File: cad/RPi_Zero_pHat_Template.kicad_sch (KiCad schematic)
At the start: 2 parts, among them J1 RPi_GPIO, J2 RPi_GPIO

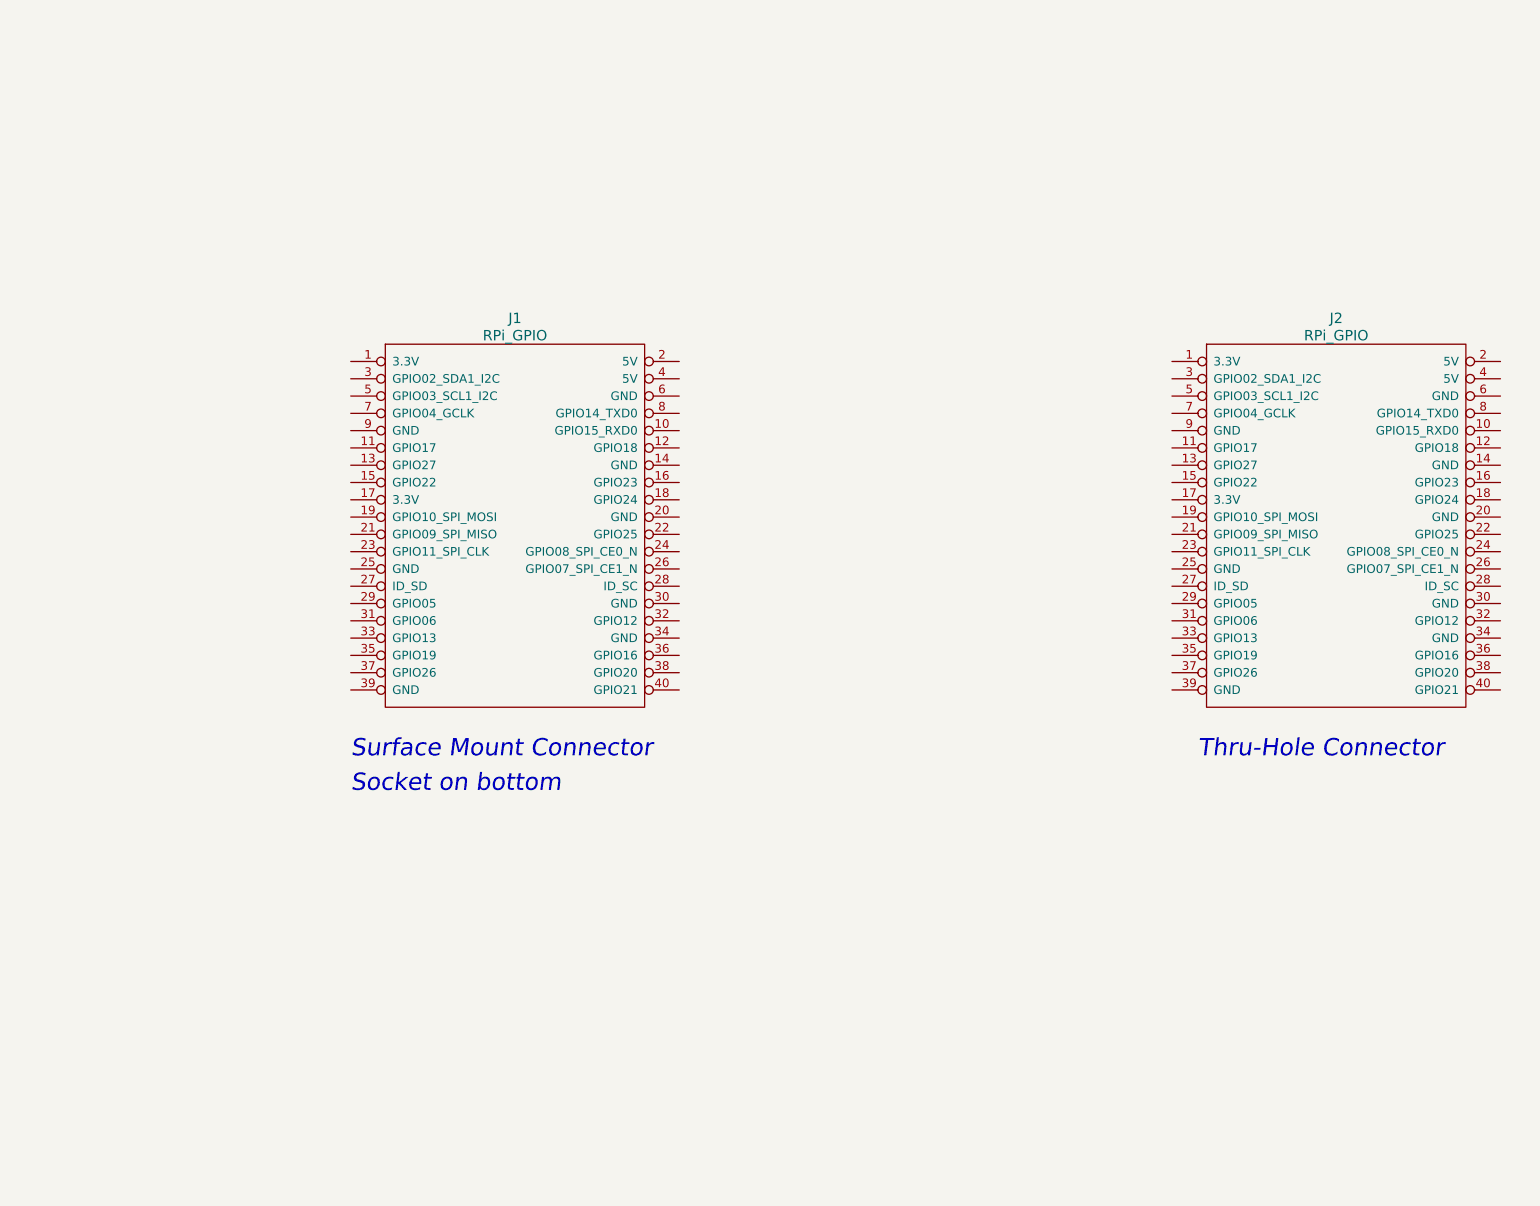
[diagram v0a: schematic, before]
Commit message: some headers added
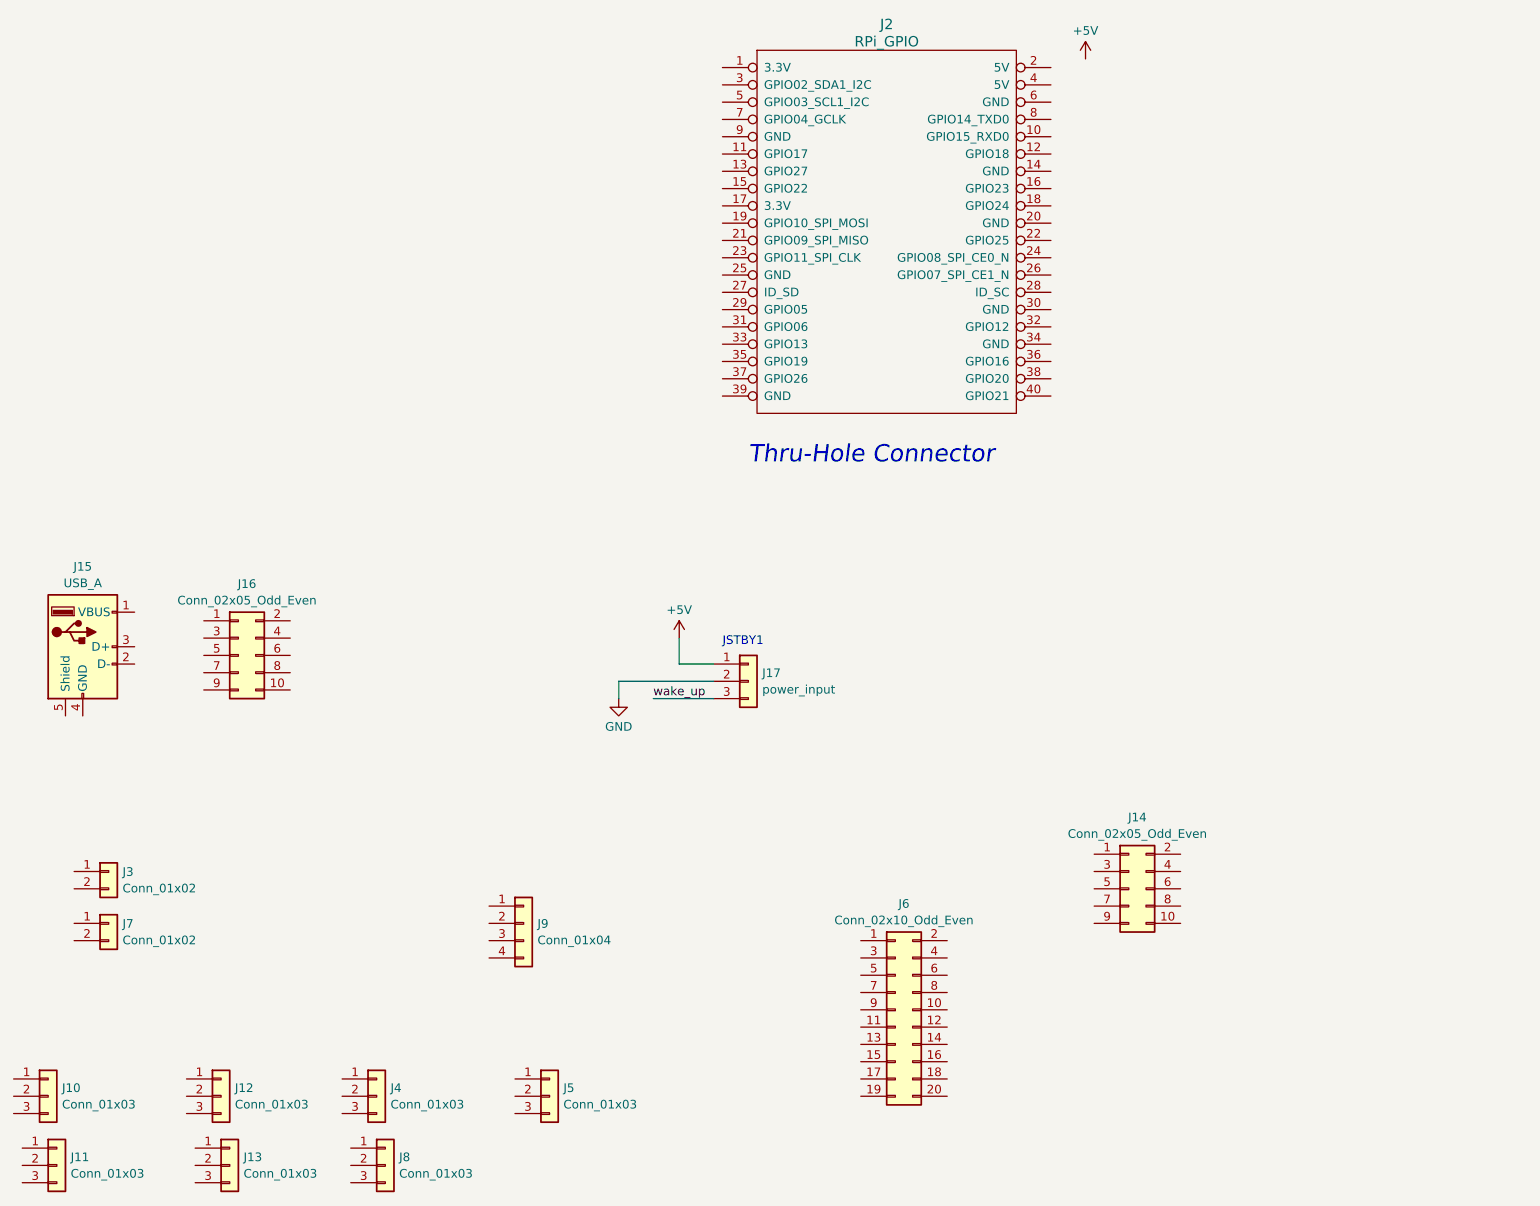
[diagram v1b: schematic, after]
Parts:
- removed J1: RPi_GPIO, RPi_Hat:Samtec_HLE-120-02-XXX-DV-BE-XX-XX, symbol RPi_Zero_pHat_Template-rescue:RPi_GPIO-Connector-ML
- added J10, J11, J12, J13, J4, J5, J8: Conn_01x03, Connector_PinHeader_2.54mm:PinHeader_1x03_P2.54mm_Vertical, symbol Connector_Generic:Conn_01x03
- added J14: Conn_02x05_Odd_Even, Connector_IDC:IDC-Header_2x05_P2.54mm_Vertical, symbol Connector_Generic:Conn_02x05_Odd_Even
- added J15: USB_A, Connector_USB:USB_A_CONNFLY_DS1095-WNR0, symbol Connector:USB_A
- added J16: Conn_02x05_Odd_Even, Connector_PinHeader_2.54mm:PinHeader_2x05_P2.54mm_Vertical, symbol Connector_Generic:Conn_02x05_Odd_Even
- added J17: power_input, Connector_PinHeader_2.54mm:PinHeader_1x03_P2.54mm_Vertical, symbol Connector_Generic:Conn_01x03
- added J3, J7: Conn_01x02, Connector_PinHeader_2.54mm:PinHeader_1x02_P2.54mm_Vertical, symbol Connector_Generic:Conn_01x02
- added J6: Conn_02x10_Odd_Even, Connector_PinHeader_2.54mm:PinHeader_2x10_P2.54mm_Vertical, symbol Connector_Generic:Conn_02x10_Odd_Even
- added J9: Conn_01x04, Connector_PinHeader_2.54mm:PinHeader_1x04_P2.54mm_Vertical, symbol Connector_Generic:Conn_01x04
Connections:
- new net +5V: J17.1 (Pin_1)
- new net GND: J17.2 (Pin_2)
- new net wake_up: J17.3 (Pin_3)
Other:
- note added: "JSTBY1"
- note removed: "Socket on bottom"
- note removed: "Surface Mount Connector"
- moved on the sheet: J2

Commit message: init
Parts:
- added D101, D102, D103, D104, D105, D106, D107, D108, D109, D110, D111, D112, D113, D114: led_g, LED_SMD:LED_0603_1608Metric, symbol Device:LED
- added R101, R102, R103, R104, R105, R106, R107, R108, R117, R118, R119, R120, R121, R122: 4.7k, Resistor_SMD:R_0603_1608Metric, symbol Device:R_Small
- added R109, R110, R111, R112, R113, R114, R115, R116, R123, R124, R125, R126, R127, R128: 10k, Resistor_SMD:R_0603_1608Metric, symbol Device:R_Small
- added U101, U102, U103, U104, U105, U106, U107, U108, U109, U110, U111, U112, U113, U114: ASSR-1218, Package_SO:SO-4_4.4x4.3mm_P2.54mm, symbol Relay_SolidState:ASSR-1218
- renumbered J10 to J101, J12 to J102, J5 to J103, J11 to J104, J4 to J105, J13 to J106, J8 to J107, J15 to J108, J3 to J109, J7 to J110, J16 to J111, J9 to J112, J17 to J113, J2 to J114, J6 to J115, J14 to J116
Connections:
- net +5V: now also J114.2 (5V), J114.4 (5V)
- net GND: now also R109.1, R110.1, R111.1, R112.1, R113.1, R114.1, R115.1, R116.1, R123.1, R124.1, R125.1, R126.1, R127.1, R128.1, U101.2, U102.2, U103.2, U104.2, U105.2, U106.2, U107.2, U108.2, U109.2, U110.2, U111.2, U112.2, U113.2, U114.2
- net at J106.1 (Pin_1): now also U111.4
- net at J106.2 (Pin_2): now also U111.3, U112.4
- net at J106.3 (Pin_3): now also U112.3
- net at J102.1 (Pin_1): now also U103.4
- net at J102.2 (Pin_2): now also U103.3, U104.4
- net at J102.3 (Pin_3): now also U104.3
- net at J101.1 (Pin_1): now also U101.4
- net at J101.2 (Pin_2): now also U101.3, U102.4
- net at J101.3 (Pin_3): now also U102.3
- net at J104.1 (Pin_1): now also U107.4
- net at J104.2 (Pin_2): now also U107.3, U108.4
- net at J104.3 (Pin_3): now also U108.3
- net at J103.1 (Pin_1): now also U105.4
- net at J103.2 (Pin_2): now also U105.3, U106.4
- net at J103.3 (Pin_3): now also U106.3
- net at J105.1 (Pin_1): now also U109.4
- net at J105.2 (Pin_2): now also U109.3, U110.4
- net at J105.3 (Pin_3): now also U110.3
- net at J107.1 (Pin_1): now also U113.4
- net at J107.2 (Pin_2): now also U113.3, U114.4
- net at J107.3 (Pin_3): now also U114.3
- new net: R102.1, U102.1
- new net: D112.1 (K), R126.2
- new net: D112.2 (A), R120.2
- new net: D113.1 (K), R127.2
- new net: R119.1, U111.1
- new net: D102.2 (A), R102.2
- new net: D105.1 (K), R113.2
- new net: R117.1, U109.1
- new net: R103.1, U103.1
- new net: D109.1 (K), R123.2
- new net: R104.1, U104.1
- new net: D104.2 (A), R104.2
- new net: R121.1, U113.1
- new net: R107.1, U107.1
- new net: D108.1 (K), R116.2
- new net: R101.1, U101.1
- new net: R105.1, U105.1
- new net: D101.1 (K), R109.2
- new net: D103.1 (K), R111.2
- new net: D107.1 (K), R115.2
- new net: R120.1, U112.1
- new net: R106.1, U106.1
- new net: D106.1 (K), R114.2
- new net: D106.2 (A), R106.2
- new net: R118.1, U110.1
- new net: R122.1, U114.1
- new net: D111.1 (K), R125.2
- new net: D102.1 (K), R110.2
- new net: D110.1 (K), R124.2
- new net: D110.2 (A), R118.2
- new net: R108.1, U108.1
- new net: D108.2 (A), R108.2
- new net: D114.1 (K), R128.2
- new net: D104.1 (K), R112.2
- new net: D114.2 (A), R122.2
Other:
- moved on the sheet: J101, J102, J103, J104, J105, J106, J107, J108, J109, J110, J111, J112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

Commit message: check in before tpm
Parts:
- added C101: .1uF, Capacitor_SMD:C_0603_1608Metric, symbol Device:C_Small
- added C102: 22uF, Capacitor_SMD:C_0805_2012Metric, symbol Device:CP_Small
- added JP101, JP102: Jumper_NC_Small, Jumper:SolderJumper-2_P1.3mm_Bridged_RoundedPad1.0x1.5mm, symbol Device:Jumper_NC_Small
- added R129, R130, R131, R132, R133, R134: 4.7k, Resistor_SMD:R_0603_1608Metric, symbol Device:R_Small
- added U1: MCP23017, Package_SO:SOIC-28W_7.5x17.9mm_P1.27mm, symbol rte:MCP23017
- added U115, U116: ASSR-1218, Package_SO:SO-4_4.4x4.3mm_P2.54mm, symbol Relay_SolidState:ASSR-1218
- J115: renamed from J114; footprint RPi_Hat:Pin_Header_Straight_2x20 -> Connector_PinHeader_2.54mm:PinHeader_2x20_P2.54mm_Vertical
- renumbered D113 to D109, D114 to D110, D109 to D111, D110 to D112, D111 to D113, D112 to D114, J107 to J105, J105 to J106, J106 to J107, J116 to J108, J110 to J109, J109 to J110, J112 to J111, J108 to J112, J111 to J113, J113 to J114, J115 to J116, R121 to R117, R122 to R118, R117 to R119, R118 to R120, R119 to R121, R120 to R122, R127 to R123, R128 to R124, R123 to R125, R124 to R126, R125 to R127, R126 to R128, U113 to U109, U114 to U110, U109 to U111, U110 to U112, U111 to U113, U112 to U114
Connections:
- net GND: now also J111.2 (Pin_2), J112.4 (GND), J112.5 (Shield), J115.14 (GND), J115.20 (GND), J115.25 (GND), J115.30 (GND), J115.34 (GND), J115.39 (GND), J115.6 (GND), J115.9 (GND), C101.1, C102.2, U1.10 (GND), U1.15 (A0), U1.16 (A1), U1.17 (A2), U115.2, U116.2
- net +3V3: now reaches J115.1 (3.3V)
- net +3V3: now also J115.17 (3.3V), C101.2, C102.1, R131.1, R132.1, R133.1, R134.1, U1.18 (~{RESET}), U1.9 (VCC)
- net RX: now reaches J115.10 (GPIO15_RXD0)
- net RX: now also J108.3 (Pin_3)
- net IO_SCL: now reaches J115.11 (GPIO17)
- net IO_SCL: now also R134.2, U1.12 (SCL)
- net IO_SDA: now reaches J115.13 (GPIO27)
- net IO_SDA: now also R133.2, U1.13 (SDA)
- net SDA: now reaches J115.3 (GPIO02_SDA1_I2C)
- net SDA: now also J111.1 (Pin_1), JP102.1
- net SCL: now reaches J115.5 (GPIO03_SCL1_I2C)
- net SCL: now also J111.3 (Pin_3), JP101.1
- net TX: now reaches J115.8 (GPIO14_TXD0)
- net TX: now also J108.5 (Pin_5)
- net E_GPA2: now reaches D114.2 (A), R122.2
- net E_GPA2: now also U1.23 (GPA2)
- net E_GPA3: now reaches R121.2
- net E_GPA3: now also U1.24 (GPA3)
- net E_GPB1: now reaches D102.2 (A), R102.2
- net E_GPB1: now also U1.2 (GPB1)
- net E_GPA5: now reaches R119.2
- net E_GPA5: now also U1.26 (GPA5)
- net E_GPB2: now reaches R103.2
- net E_GPB2: now also U1.3 (GPB2)
- net at J109.1 (Pin_1): now also U115.4
- net at J109.2 (Pin_2): now also U115.3
- net E_GPB3: now reaches D104.2 (A), R104.2
- net E_GPB3: now also U1.4 (GPB3)
- net at J113.3 (Pin_3): now also J112.2 (D-)
- net at J113.5 (Pin_5): now also J112.3 (D+)
- net E_GPA1: now reaches R117.2
- net E_GPA1: now also U1.22 (GPA1)
- net E_GPB7: now reaches R107.2
- net E_GPB7: now also U1.8 (GPB7)
- net E_GPB5: now reaches D106.2 (A), R106.2
- net E_GPB5: now also U1.6 (GPB5)
- net at J110.1 (Pin_1): now also U116.4
- net at J110.2 (Pin_2): now also U116.3
- net E_GPB4: now reaches R105.2
- net E_GPB4: now also U1.5 (GPB4)
- net E_GPB0: now reaches R101.2
- net E_GPB0: now also U1.1 (GPB0)
- net E_GPA4: now reaches D112.2 (A), R120.2
- net E_GPA4: now also U1.25 (GPA4)
- net E_GPB6: now reaches D108.2 (A), R108.2
- net E_GPB6: now also U1.7 (GPB6)
- net E_GPA0: now reaches D110.2 (A), R118.2
- net E_GPA0: now also U1.21 (GPA0)
- new net: JP102.2, R132.2
- new net: R130.1, U116.1
- new net: R129.1, U115.1
- new net: JP101.2, R131.2
- new net E_GPA6: R129.2, U1.27 (GPA6)
- new net E_GPA7: R130.2, U1.28 (GPA7)
- new net PA_EINT10: U1.20 (INTA)
- new net PA_EINT7: U1.19 (INTB)
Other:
- note added: "4-pin BMC I2C"
- note added: "GPIO EXPANDER"
- note added: "PWR"
- note added: "RESET"
- note added: "SERIAL"
- note added: "TPM"
- moved on the sheet: J108, J109, J110, J111, J113
